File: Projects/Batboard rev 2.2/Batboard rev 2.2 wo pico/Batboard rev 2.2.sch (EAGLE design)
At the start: 61 parts, among them J1 1X2-3.5MM, J2 1X2-3.5MM, J3 1X2-3.5MM, J4 1X2-3.5MM, J5 1X2-3.5MM, J6 1X2-3.5MM, U2 TL3472CD, X1 22-23-2081, X17 22-23-2081

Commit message: Updated
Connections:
- removed net 12V: C2.2, U$5.VCC
- net +12V: now also C2.2, U$5.VCC
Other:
- moved on the sheet: C16, C17, C18, C20, C21, R12, R9, SLF1

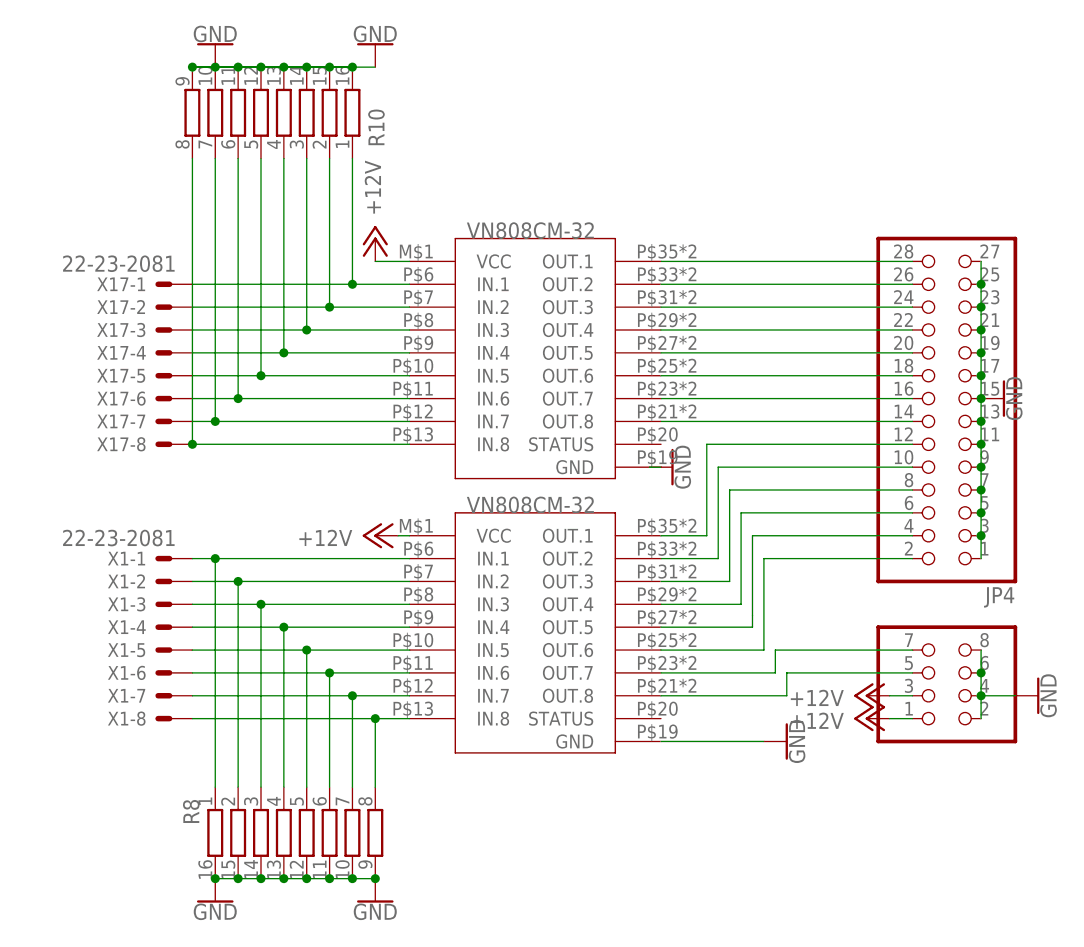
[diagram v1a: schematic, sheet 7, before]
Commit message: Checked ERC and DRC
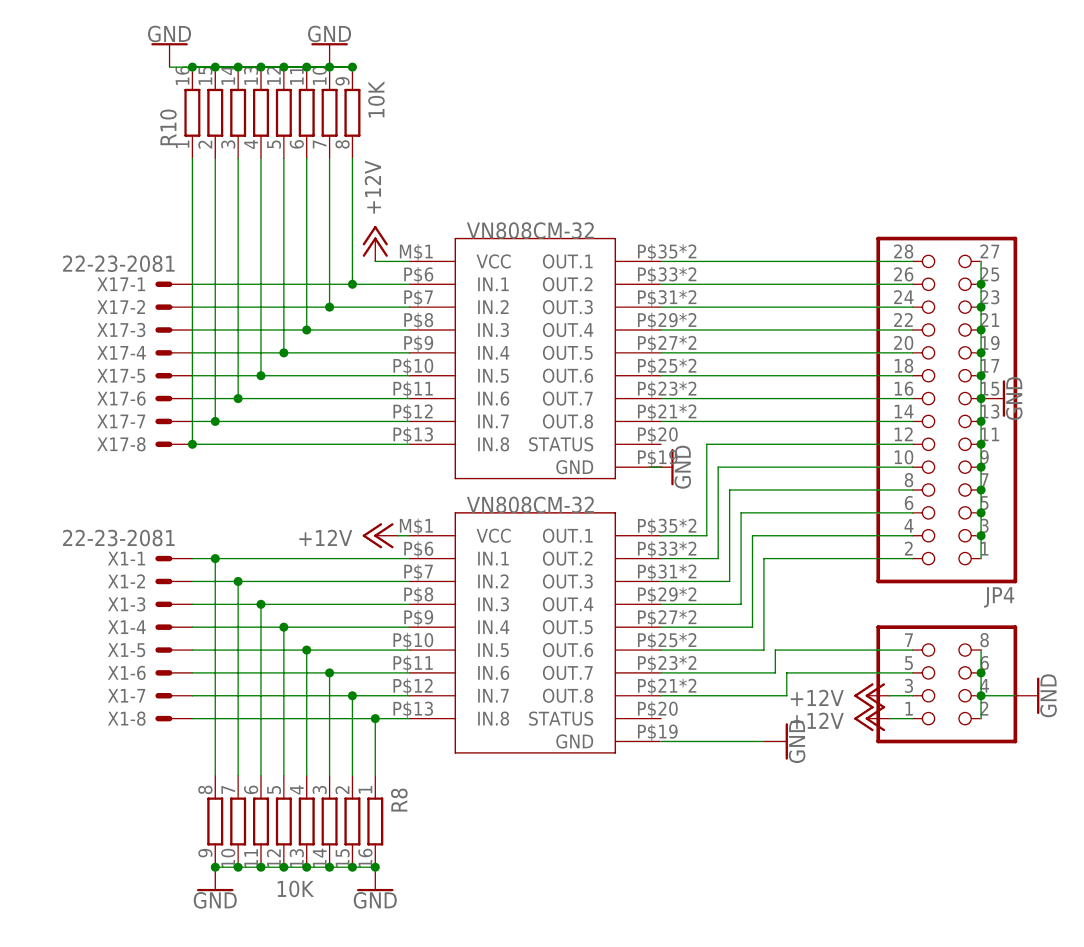
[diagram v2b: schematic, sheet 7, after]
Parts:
- added U$6: XT60, ultravolt_daughterboard:XT60
- added U$8: DMN2004DMK_DUAL_N-CHANNEL_MOSFET_ARRAY, ultravolt_daughterboard:DMN2004DMK_DUAL_N-CHANNEL_MOSFET_ARRAY
- R10, R8: value (none) -> 10K
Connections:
- removed net N$31: U$5.GND
- net BATT: now also U$6.1
- net GND: now also U$5.GND, U$6.2
- net N$2: now also R10.8; no longer R10.1
- net N$3: now also R10.7; no longer R10.2
- net N$30: now also R8.8; no longer R8.1
- net N$32: now also R10.1; no longer R10.8
- net N$33: now also R10.2; no longer R10.7
- net N$35: now also R10.6; no longer R10.3
- net N$36: now also R10.3; no longer R10.6
- net N$37: now also R10.4; no longer R10.5
- net N$38: now also R10.5; no longer R10.4
- net N$39: now also R8.1; no longer R8.8
- net N$40: now also R8.2; no longer R8.7
- net N$41: now also R8.7; no longer R8.2
- net N$42: now also R8.6; no longer R8.3
- net N$43: now also R8.3; no longer R8.6
- net N$44: now also R8.4; no longer R8.5
- net N$45: now also R8.5; no longer R8.4
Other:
- moved on the sheet: R8

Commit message: BOM generation started
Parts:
- added SV1: (no value), con-lstb:MA03-1
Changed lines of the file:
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@@
 <part name="GND5" library="SparkFun-PowerSymbols" library_urn="urn:adsk.eagle:library:530" deviceset="GND" device=""/>
 <part name="U$8" library="ultravolt_daughterboard" deviceset="DMN2004DMK_DUAL_N-CHANNEL_MOSFET_ARRAY" device=""/>
+<part name="SV1" library="con-lstb" library_urn="urn:adsk.eagle:library:162" deviceset="MA03-1" device="" package3d_urn="urn:adsk.eagle:package:8339/1"/>
 </parts>
 <sheets>
@@
 <instance part="U$6" gate="G$1" x="-31.75" y="-60.96"/>
 <instance part="U$8" gate="G$1" x="21.59" y="-7.62"/>
+<instance part="SV1" gate="G$1" x="30.48" y="-39.37" rot="R180"/>
 </instances>
 <busses>

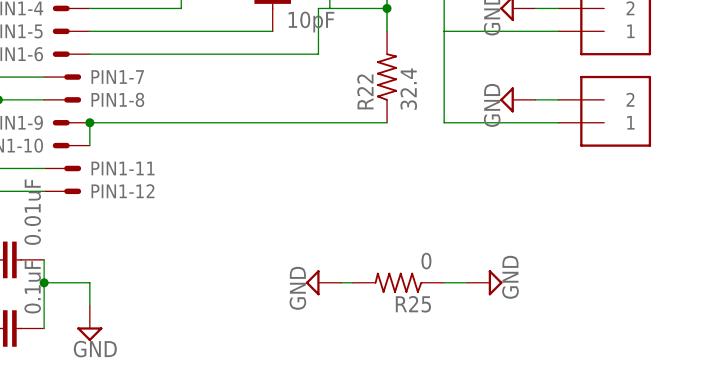
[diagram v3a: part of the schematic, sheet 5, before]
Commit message: Updated capacitors for switching step down regulators
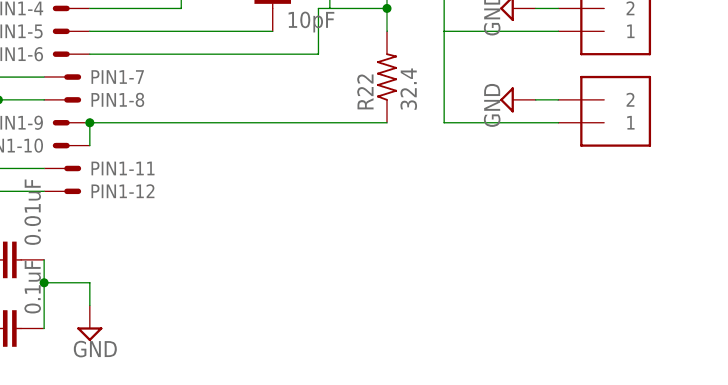
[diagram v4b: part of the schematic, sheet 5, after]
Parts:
- removed C21: 100uF, SparkFun-Capacitors:1.0UF-1206-50V-10%
- removed R25: 0, adafruit:R-US_M1206
- added C15: 100uF, SparkFun-Capacitors:100UF-POLAR-25V-20%(ELEC)
- C9: value 13.9uF -> 100uF; device SparkFun-Capacitors:1.0UF-1206-50V-10% -> SparkFun-Capacitors:100UF-POLAR-25V-20%(ELEC); MF KEMET -> (none); MPN C0805C103K1RACTU -> (none); OC_FARNELL 1414661 -> (none)
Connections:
- net +12V: now also C9.+; no longer C9.1
- net +5V: now also C15.+; no longer C21.2
- net GND: now also C15.-, C9.-; no longer C21.1, C9.2, R25.1, R25.2
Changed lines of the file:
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@@
 <attribute name="OC_FARNELL" value="1100322"/>
 </part>
-<part name="R25" library="adafruit" library_urn="urn:adsk.eagle:library:420" deviceset="R-US_" device="M1206" value="0">
-<attribute name="MF" value="PANASONIC ELECTRONIC COMPONENTS"/>
-<attribute name="MPN" value="ERJ8ENF32R4V"/>
-<attribute name="OC_FARNELL" value="2307627"/>
-</part>
-<part name="SUPPLY24" library="supply2" library_urn="urn:adsk.eagle:library:372" deviceset="GND" device=""/>
-<part name="SUPPLY25" library="supply2" library_urn="urn:adsk.eagle:library:372" deviceset="GND" device=""/>
 <part name="U$1" library="ultravolt_daughterboard" deviceset="HV_DC_BOARD_SOCKET" device=""/>
 <part name="SUPPLY1" library="supply2" library_urn="urn:adsk.eagle:library:372" deviceset="V+" device="" value="400V"/>
@@
 <part name="GND34" library="SparkFun-PowerSymbols" library_urn="urn:adsk.eagle:library:530" deviceset="GND" device=""/>
 <part name="P+11" library="supply1" library_urn="urn:adsk.eagle:library:371" deviceset="+12V" device=""/>
-<part name="C9" library="SparkFun-Capacitors" library_urn="urn:adsk.eagle:library:510" deviceset="1.0UF" device="-1206-50V-10%" package3d_urn="urn:adsk.eagle:package:37426/1" value="13.9uF">
-<attribute name="MF" value="KEMET"/>
-<attribute name="MPN" value="C0805C103K1RACTU"/>
-<attribute name="OC_FARNELL" value="1414661"/>
-</part>
 <part name="GND35" library="SparkFun-PowerSymbols" library_urn="urn:adsk.eagle:library:530" deviceset="GND" device=""/>
 <part name="GND36" library="SparkFun-PowerSymbols" library_urn="urn:adsk.eagle:library:530" deviceset="GND" device=""/>
@@
 <part name="P+8" library="supply1" library_urn="urn:adsk.eagle:library:371" deviceset="+5V" device=""/>
 <part name="GND31" library="SparkFun-PowerSymbols" library_urn="urn:adsk.eagle:library:530" deviceset="GND" device=""/>
-<part name="C21" library="SparkFun-Capacitors" library_urn="urn:adsk.eagle:library:510" deviceset="1.0UF" device="-1206-50V-10%" package3d_urn="urn:adsk.eagle:package:37426/1" value="100uF">
-<attribute name="MF" value="KEMET"/>
-<attribute name="MPN" value="C0805C103K1RACTU"/>
-<attribute name="OC_FARNELL" value="1414661"/>
-</part>
 <part name="U$6" library="ultravolt_daughterboard" deviceset="XT60" device=""/>
 <part name="R8" library="resistor-bourns" library_urn="urn:adsk.eagle:library:341" deviceset="4816P-T01" device="" package3d_urn="urn:adsk.eagle:package:24859/1" value="10K"/>
@@
 <part name="U$8" library="ultravolt_daughterboard" deviceset="DMN2004DMK_DUAL_N-CHANNEL_MOSFET_ARRAY" device=""/>
 <part name="SV1" library="con-lstb" library_urn="urn:adsk.eagle:library:162" deviceset="MA03-1" device="" package3d_urn="urn:adsk.eagle:package:8339/1"/>
+<part name="C15" library="SparkFun-Capacitors" library_urn="urn:adsk.eagle:library:510" deviceset="100UF-POLAR" device="-25V-20%(ELEC)" package3d_urn="urn:adsk.eagle:package:37420/1" value="100uF"/>
+<part name="C9" library="SparkFun-Capacitors" library_urn="urn:adsk.eagle:library:510" deviceset="100UF-POLAR" device="-25V-20%(ELEC)" package3d_urn="urn:adsk.eagle:package:37420/1" value="100uF"/>
 </parts>
 <sheets>
@@
 <instance part="GND34" gate="1" x="-44.45" y="19.05" rot="R270"/>
 <instance part="P+11" gate="1" x="48.26" y="49.53" rot="R270"/>
-<instance part="C9" gate="G$1" x="39.37" y="44.45" smashed="yes">
-<attribute name="OC_FARNELL" x="39.37" y="44.45" size="1.778" layer="96" rot="R270" display="off"/>
-<attribute name="MF" x="39.37" y="44.45" size="1.778" layer="96" rot="R270" display="off"/>
-<attribute name="MPN" x="39.37" y="44.45" size="1.778" layer="96" rot="R270" display="off"/>
-<attribute name="NAME" x="40.894" y="47.371" size="1.778" layer="95" font="vector"/>
-<attribute name="VALUE" x="40.894" y="42.291" size="1.778" layer="96" font="vector"/>
-</instance>
 <instance part="GND35" gate="1" x="39.37" y="36.83"/>
 <instance part="GND36" gate="1" x="45.72" y="19.05" rot="R90"/>
 <instance part="GND37" gate="1" x="25.4" y="30.48" rot="R180"/>
 <instance part="GND39" gate="1" x="-38.1" y="26.67" rot="R270"/>
+<instance part="C9" gate="G$1" x="39.37" y="46.99"/>
 </instances>
 <busses>
@@
 </segment>
 <segment>
-<pinref part="C9" gate="G$1" pin="2"/>
 <pinref part="GND35" gate="1" pin="GND"/>
 <wire x1="39.37" y1="39.37" x2="39.37" y2="41.91" width="0.1524" layer="91"/>
+<pinref part="C9" gate="G$1" pin="-"/>
 </segment>
 <segment>
@@
 <junction x="30.48" y="49.53"/>
 <pinref part="P+11" gate="1" pin="+12V"/>
-<pinref part="C9" gate="G$1" pin="1"/>
+<pinref part="C9" gate="G$1" pin="+"/>
 <junction x="39.37" y="49.53"/>
 </segment>
@@
 <attribute name="VALUE" x="43.434" y="26.67" size="1.778" layer="96" rot="R90" align="top-center"/>
 </instance>
-<instance part="C21" gate="G$1" x="38.1" y="19.05" smashed="yes">
-<attribute name="OC_FARNELL" x="38.1" y="19.05" size="1.778" layer="96" rot="R270" display="off"/>
-<attribute name="MF" x="38.1" y="19.05" size="1.778" layer="96" rot="R270" display="off"/>
-<attribute name="MPN" x="38.1" y="19.05" size="1.778" layer="96" rot="R270" display="off"/>
-<attribute name="NAME" x="40.894" y="21.971" size="1.778" layer="95" font="vector"/>
-<attribute name="VALUE" x="39.624" y="16.891" size="1.778" layer="96" font="vector"/>
-</instance>
+<instance part="C15" gate="G$1" x="38.1" y="19.05" rot="R180"/>
 </instances>
 <busses>
@@
 <wire x1="35.56" y1="26.67" x2="38.1" y2="26.67" width="0.1524" layer="91"/>
 <pinref part="GND31" gate="1" pin="GND"/>
-<pinref part="C21" gate="G$1" pin="1"/>
 <wire x1="38.1" y1="26.67" x2="40.64" y2="26.67" width="0.1524" layer="91"/>
 <wire x1="38.1" y1="24.13" x2="38.1" y2="26.67" width="0.1524" layer="91"/>
 <junction x="38.1" y="26.67"/>
+<pinref part="C15" gate="G$1" pin="-"/>
 </segment>
 </net>
@@
 <junction x="25.4" y="13.97"/>
 <pinref part="P+8" gate="1" pin="+5V"/>
-<pinref part="C21" gate="G$1" pin="2"/>
 <wire x1="38.1" y1="13.97" x2="50.8" y2="13.97" width="0.1524" layer="91"/>
 <wire x1="38.1" y1="16.51" x2="38.1" y2="13.97" width="0.1524" layer="91"/>
 <junction x="38.1" y="13.97"/>
+<pinref part="C15" gate="G$1" pin="+"/>
 </segment>
 </net>
@@
 <attribute name="VALUE" x="-72.898" y="-6.35" size="1.778" layer="96" rot="R90"/>
 </instance>
-<instance part="R25" gate="G$1" x="67.31" y="-27.94" smashed="yes" rot="R180">
-<attribute name="OC_FARNELL" x="67.31" y="-27.94" size="1.778" layer="96" rot="R90" display="off"/>
-<attribute name="MF" x="67.31" y="-27.94" size="1.778" layer="96" rot="R90" display="off"/>
-<attribute name="MPN" x="67.31" y="-27.94" size="1.778" layer="96" rot="R90" display="off"/>
-<attribute name="NAME" x="71.12" y="-29.4386" size="1.778" layer="95" rot="R180"/>
-<attribute name="VALUE" x="71.12" y="-24.638" size="1.778" layer="96" rot="R180"/>
-</instance>
-<instance part="SUPPLY24" gate="GND" x="58.42" y="-27.94" smashed="yes" rot="R270">
-<attribute name="VALUE" x="55.245" y="-26.035" size="1.778" layer="96" rot="R270"/>
-</instance>
-<instance part="SUPPLY25" gate="GND" x="77.47" y="-27.94" smashed="yes" rot="R90">
-<attribute name="VALUE" x="80.645" y="-29.845" size="1.778" layer="96" rot="R90"/>
-</instance>
 <instance part="R2" gate="G$1" x="-41.91" y="43.18" rot="R270"/>
 <instance part="SUPPLY2" gate="GND" x="80.01" y="-7.62" smashed="yes" rot="R270">
@@
 </segment>
 <segment>
-<pinref part="R25" gate="G$1" pin="1"/>
-<pinref part="SUPPLY25" gate="GND" pin="GND"/>
-<wire x1="74.93" y1="-27.94" x2="72.39" y2="-27.94" width="0.1524" layer="91"/>
-</segment>
-<segment>
-<pinref part="R25" gate="G$1" pin="2"/>
-<pinref part="SUPPLY24" gate="GND" pin="GND"/>
-<wire x1="60.96" y1="-27.94" x2="62.23" y2="-27.94" width="0.1524" layer="91"/>
-</segment>
-<segment>

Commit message: Not sure
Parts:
- added LED1, LED2, LED3, LED4: (no value), eagle-ltspice:LED_E
- added R1, R11, R13, R4: 1K, adafruit:R-US_M1206
- added U$9: DMN2004DMK_DUAL_N-CHANNEL_MOSFET_ARRAY, ultravolt_daughterboard:DMN2004DMK_DUAL_N-CHANNEL_MOSFET_ARRAY
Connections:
- new net 10V: U$1.PGRM, U$1.REF, U$8.G1
- new net N$31: LED1.A, U$8.D
- new net N$84: LED2.A, U$8.D1
- new net N$85: LED3.A, U$9.D
- new net N$86: LED4.A, U$9.D1
- new net N$87: LED2.C, R4.2
- new net N$88: LED3.C, R11.2
- new net N$89: LED4.C, R13.2
- net +12V: now also U$9.G
- net +5V: now also R1.1, R11.1, R4.1, U$8.G, U$9.G1
- net -12V: now also U$9.S1
- net GND: now also R13.1, U$8.S, U$8.S1, U$9.S
- net N$1: now also LED1.C, R1.2; no longer U$1.PGRM, U$1.REF
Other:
- moved on the sheet: U$8

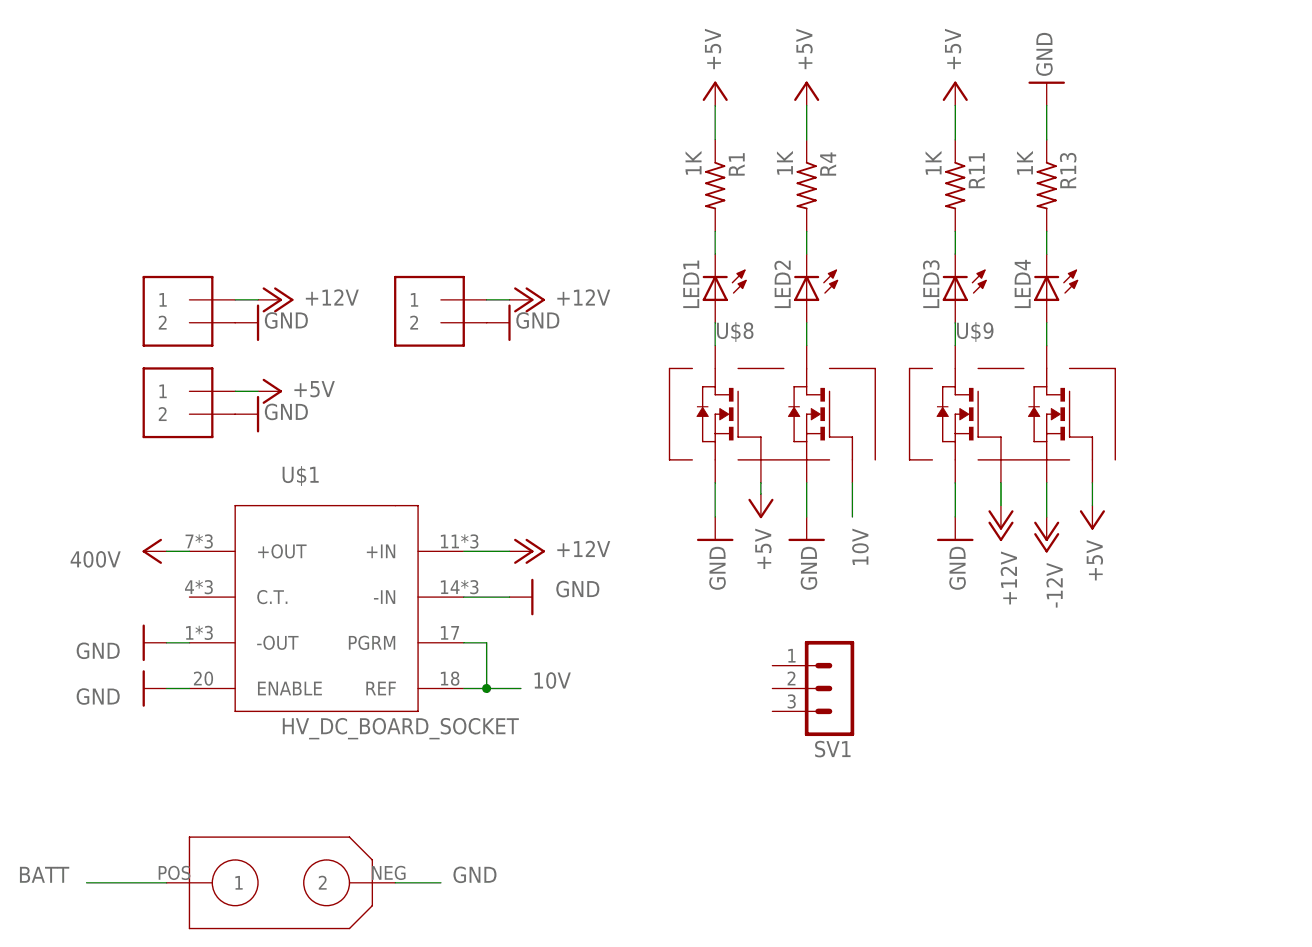
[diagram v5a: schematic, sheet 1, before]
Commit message: Fixed back to "Updated LEDs"
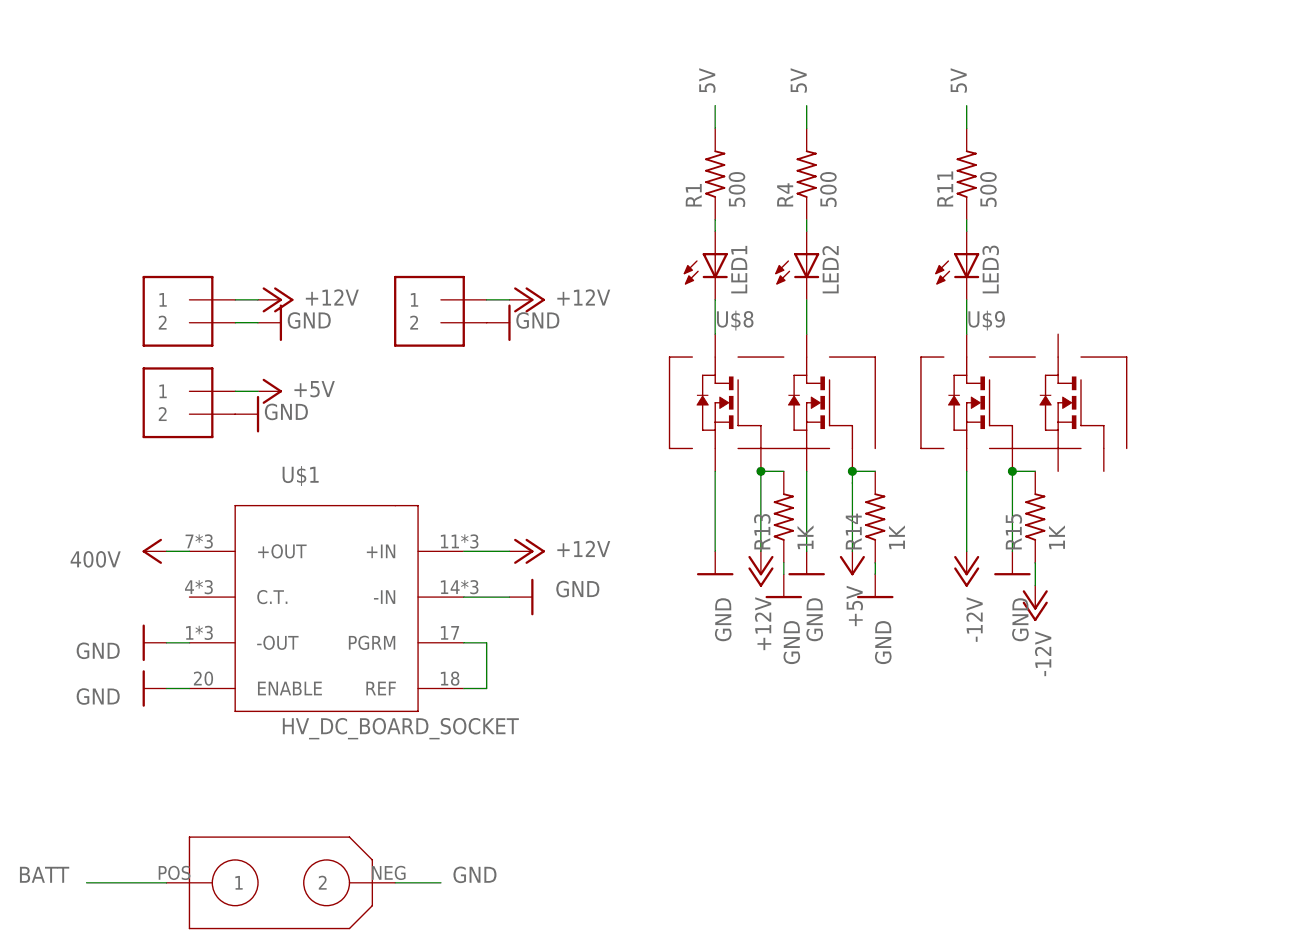
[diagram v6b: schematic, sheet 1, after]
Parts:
- removed LED4: (no value), eagle-ltspice:LED_E
- removed SV1: (no value), con-lstb:MA03-1
- added R14, R15: 1K, resistor:R-US_R1206
- R1, R11, R4: value 1K -> 500; device adafruit:R-US_M1206 -> resistor:R-US_R1206; MF WELWYN -> (none); MPN WCR0805-18KFI -> (none); OC_FARNELL 1100322 -> (none)
- R13: device adafruit:R-US_M1206 -> resistor:R-US_R1206; MF WELWYN -> (none); MPN WCR0805-18KFI -> (none); OC_FARNELL 1100322 -> (none)
- R2: value (none) -> 50K
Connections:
- removed net 10V: U$1.PGRM, U$1.REF, U$8.G1
- removed net N$89: LED4.C, R13.2
- new net 5V: R1.2, R11.2, R4.2
- net +12V: now also R13.2, U$8.G; no longer U$9.G
- net +5V: now also R14.2, U$8.G1; no longer R1.1, R11.1, R4.1, U$8.G, U$9.G1
- net -12V: now also R15.1, U$9.S; no longer U$9.S1
- net GND: now also R14.1, R15.2, U$9.G; no longer U$9.S
- net N$1: now also U$1.PGRM, U$1.REF; no longer LED1.C, R1.2
- net N$31: now also R1.1; no longer U$8.D
- net N$84: now also R4.1; no longer U$8.D1
- net N$85: now also R11.1; no longer U$9.D
- net N$86: now also LED3.C, U$9.D; no longer LED4.A, U$9.D1
- net N$87: now also LED1.C, U$8.D; no longer LED2.C, R4.2
- net N$88: now also LED2.C, U$8.D1; no longer LED3.C, R11.2
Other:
- moved on the sheet: LED1, LED2, LED3, R1, R11, R13, R4, U$8, U$9, U2
